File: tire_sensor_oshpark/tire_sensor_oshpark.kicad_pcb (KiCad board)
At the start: 4 copper layers, 33 x 26 mm, 40 parts, among them J1 Conn_02x05_Odd_Even, U2 DPS368, U3 LIS3DHTR, X1 32MHz, X2 32.768kHz

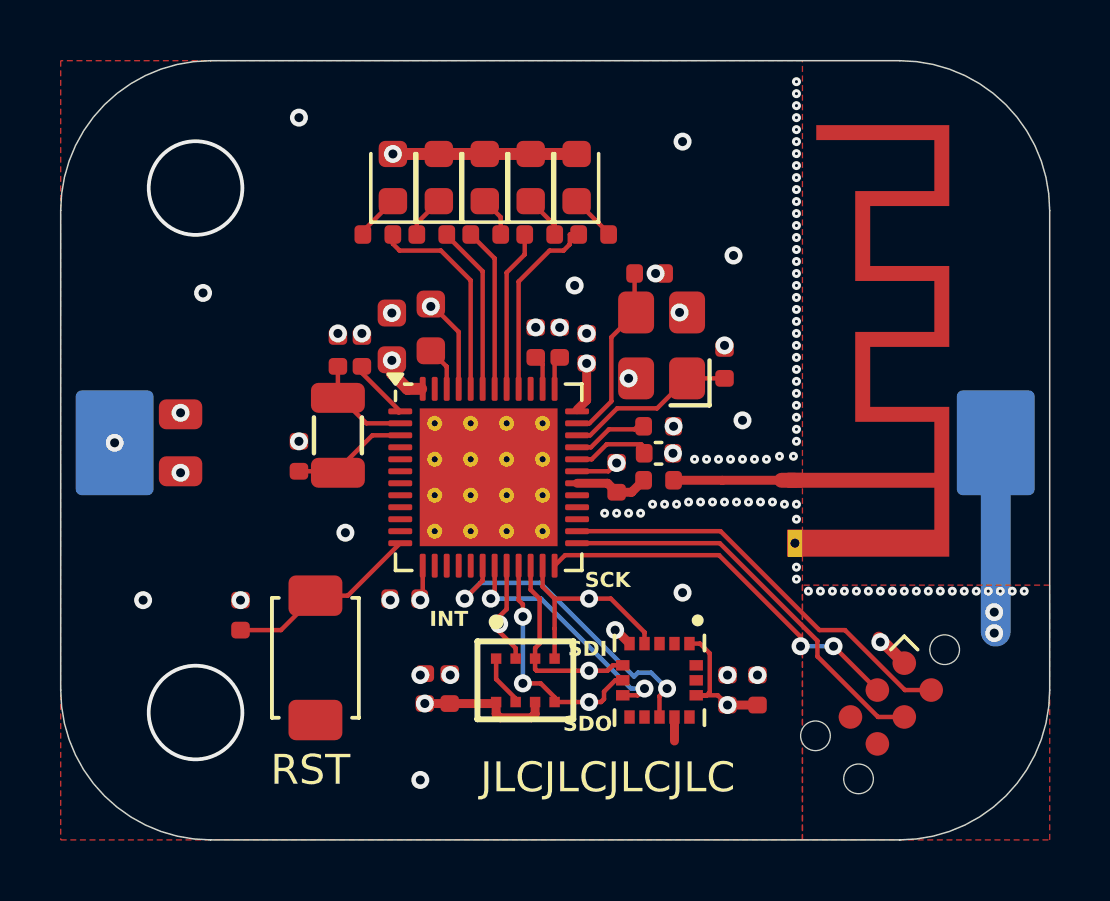
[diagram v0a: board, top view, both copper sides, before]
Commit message: Add OSHPark version, wider spacing
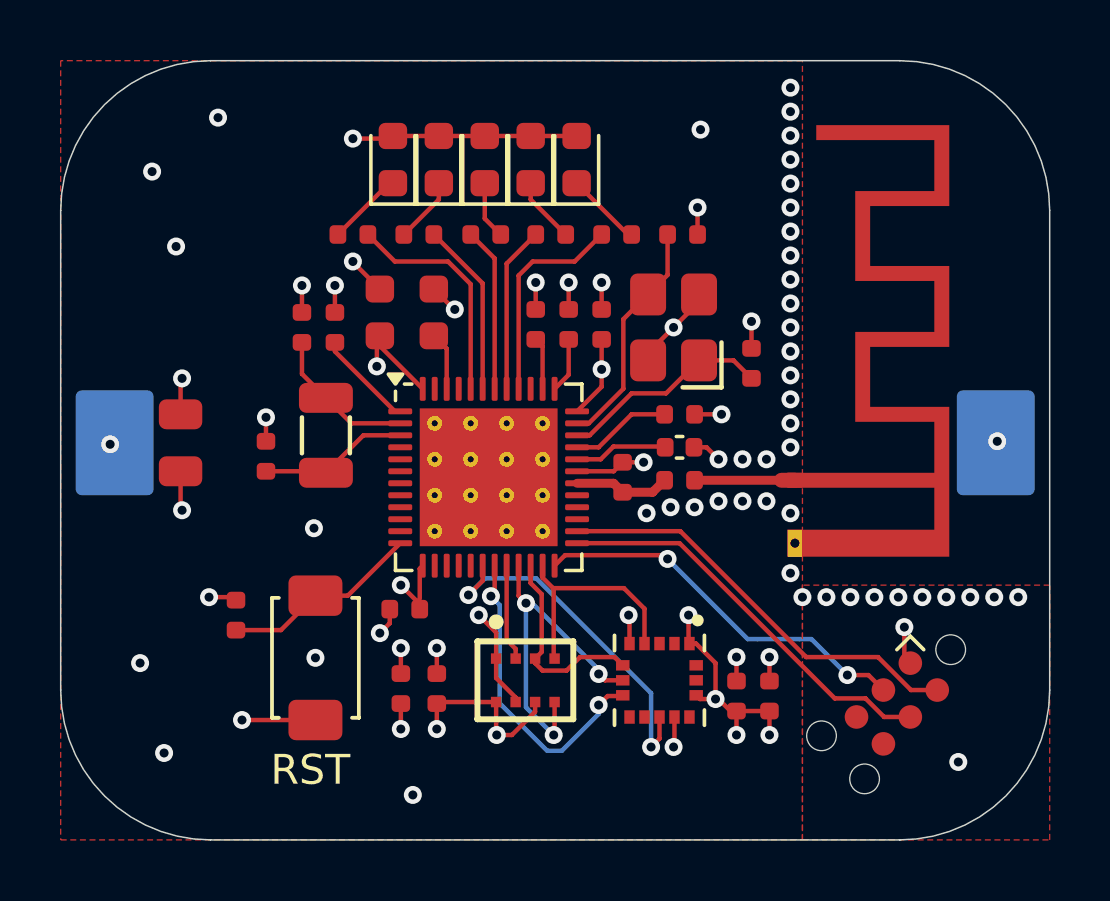
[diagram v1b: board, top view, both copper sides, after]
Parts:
- moved C2 1.70 mm to (176.6, 97.7)
- moved C11 1.44 mm to (163.9, 100.8)
- moved C4 1.20 mm to (165.0, 100.8)
- moved C12 1.10 mm to (162.7, 105.1)
- moved C8 0.94 mm to (173.9, 100.7)
- moved C1 0.90 mm to (178.9, 102.0)
- moved C9 0.89 mm to (166.5, 100.3)
- moved R5 0.83 mm to (165.6, 97.7)
- moved C7 0.81 mm to (176.5, 103.7)
- moved C19 0.80 mm to (167.2, 112.8)
- moved R1 0.77 mm to (174.4, 97.7)
- moved C6 0.73 mm to (176.5, 104.8)
- moved X1 0.72 mm to (176.3, 100.8)
- moved L1 0.70 mm to (176.5, 105.9)
- moved C13 0.67 mm to (172.8, 100.7)
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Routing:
- net GND: track 14.5 -> 29.6 mm, vias 115 -> 71
- net VDD_NRF: track 22.9 -> 33.6 mm, vias 10 -> 15
- net /SDO: track 8.12 -> 11.7 mm
- net /CS_LIS3DHTR: track 8.48 -> 10.5 mm
- net /XC2: track 6.08 -> 7.78 mm
- net /XC1: track 5.71 -> 7.10 mm
- net /P0.00/XL1: track 3.62 -> 5.01 mm
- net /P0.01/XL2: track 3.88 -> 5.02 mm
- net /DEC1: track 2.20 -> 3.31 mm
- net /INT_LIS3DHTR: track 10.9 -> 12.0 mm
- net Net-(D5-K): track 1.53 -> 2.54 mm
- net Net-(D1-K): track 1.55 -> 2.54 mm
- net /DEC3: track 2.59 -> 3.38 mm
- net Net-(D4-K): track 1.42 -> 2.20 mm
- net /RF: track 4.12 -> 3.35 mm
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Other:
- board text removed: "INT"
- board text removed: "JLCJLCJLCJLC"
- board text removed: "SCK"
- board text removed: "SDI"
- board text removed: "SDO"

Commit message: Fix VDD decoupling, reference docs
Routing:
- net VDD_NRF: track 33.6 -> 35.8 mm, vias 15 -> 12
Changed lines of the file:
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@@
-	)
-	(segment
-		(start 170.87156 114.390685)
-		(end 170.36656 114.390685)
-		(width 0.15)
-		(layer "F.Cu")
-		(net 1)
 	)
 	(segment
@@
 	)
 	(segment
-		(start 177.66656 113.190685)
-		(end 177.14656 113.190685)
-		(width 0.15)
-		(layer "F.Cu")
-		(net 1)
-	)
-	(segment
-		(start 178.36656 113.590685)
-		(end 178.16656 113.590685)
-		(width 0.15)
-		(layer "F.Cu")
-		(net 1)
-	)
-	(segment
 		(start 167.79656 109.840685)
 		(end 167.79656 108.840685)
@@
 	)
 	(segment
-		(start 176.79656 111.340685)
-		(end 177.01656 111.340685)
+		(start 177.96656 113.590685)
+		(end 178.36656 113.590685)
 		(width 0.15)
 		(layer "F.Cu")
@@
 	)
 	(segment
+		(start 177.11656 111.340685)
+		(end 177.56656 111.790685)
+		(width 0.15)
+		(layer "F.Cu")
+		(net 1)
+	)
+	(segment
+		(start 176.79656 111.340685)
+		(end 177.11656 111.340685)
+		(width 0.15)
+		(layer "F.Cu")
+		(net 1)
+	)
+	(segment
 		(start 173.86656 102.770685)
 		(end 173.86656 102.190685)
@@
 	)
 	(segment
-		(start 177.66656 111.990685)
-		(end 177.66656 113.190685)
-		(width 0.15)
-		(layer "F.Cu")
-		(net 1)
-	)
-	(segment
 		(start 177.14656 113.190685)
 		(end 177.02156 113.065685)
@@
 	)
 	(segment
-		(start 176.76656 110.390685)
-		(end 176.76656 111.310685)
-		(width 0.15)
-		(layer "F.Cu")
-		(net 1)
-	)
-	(segment
 		(start 168.36656 113.340685)
 		(end 168.36656 114.190685)
@@
 	)
 	(segment
+		(start 168.36656 113.340685)
+		(end 168.71756 113.691685)
+		(width 0.15)
+		(layer "F.Cu")
+		(net 1)
+	)
+	(segment
+		(start 173.36656 101.990685)
+		(end 173.36656 101.690685)
+		(width 0.15)
+		(layer "F.Cu")
+		(net 1)
+	)
+	(segment
 		(start 166.81406 94.490685)
 		(end 166.90156 94.403185)
@@
 	)
 	(segment
-		(start 171.64656 113.290685)
-		(end 171.64656 113.615685)
-		(width 0.15)
-		(layer "F.Cu")
-		(net 1)
-	)
-	(segment
 		(start 166.36656 102.090685)
 		(end 166.36656 101.170685)
@@
 	)
 	(segment
+		(start 177.56656 113.190685)
+		(end 177.14656 113.190685)
+		(width 0.15)
+		(layer "F.Cu")
+		(net 1)
+	)
+	(segment
+		(start 171.64656 113.615685)
+		(end 171.64656 113.290685)
+		(width 0.15)
+		(layer "F.Cu")
+		(net 1)
+	)
+	(segment
+		(start 171.57056 113.691685)
+		(end 171.64656 113.615685)
+		(width 0.15)
+		(layer "F.Cu")
+		(net 1)
+	)
+	(segment
 		(start 167.79656 110.020685)
 		(end 167.79656 110.190685)
@@
 	)
 	(segment
+		(start 168.71756 113.691685)
+		(end 171.57056 113.691685)
+		(width 0.15)
+		(layer "F.Cu")
+		(net 1)
+	)
+	(segment
 		(start 179.46656 114.390685)
 		(end 179.46656 113.590685)
@@
 	)
 	(segment
+		(start 177.56656 111.790685)
+		(end 177.56656 113.190685)
+		(width 0.15)
+		(layer "F.Cu")
+		(net 1)
+	)
+	(segment
 		(start 173.04656 103.590685)
 		(end 173.86656 102.770685)
@@
 	)
 	(segment
-		(start 170.34656 113.290685)
-		(end 170.34656 114.370685)
-		(width 0.15)
-		(layer "F.Cu")
-		(net 1)
-	)
-	(segment
-		(start 171.64656 113.615685)
-		(end 170.87156 114.390685)
+		(start 173.36656 101.690685)
+		(end 173.86656 101.190685)
 		(width 0.15)
 		(layer "F.Cu")
@@
 	(segment
 		(start 167.16656 113.340685)
+		(end 168.36656 113.340685)
+		(width 0.15)
+		(layer "F.Cu")
+		(net 1)
+	)
+	(segment
+		(start 167.16656 113.340685)
 		(end 167.16656 114.190685)
-		(width 0.15)
-		(layer "F.Cu")
-		(net 1)
-	)
-	(segment
-		(start 178.16656 113.590685)
-		(end 177.76656 113.190685)
 		(width 0.15)
 		(layer "F.Cu")
@@
 	)
 	(segment
-		(start 177.01656 111.340685)
-		(end 177.66656 111.990685)
-		(width 0.15)
-		(layer "F.Cu")
-		(net 1)
-	)
-	(segment
-		(start 170.34656 114.370685)
-		(end 170.36656 114.390685)
-		(width 0.15)
-		(layer "F.Cu")
-		(net 1)
-	)
-	(segment
 		(start 166.36656 101.170685)
 		(end 166.46656 101.070685)
@@
 	)
 	(segment
+		(start 177.56656 113.190685)
+		(end 177.96656 113.590685)
+		(width 0.15)
+		(layer "F.Cu")
+		(net 1)
+	)
+	(segment
 		(start 173.86656 101.190685)
 		(end 173.86656 102.190685)
@@
 	)
 	(via
-		(at 170.36656 114.390685)
-		(size 0.6)
-		(drill 0.3)
-		(layers "F.Cu" "B.Cu")
-		(free yes)
-		(net 1)
-	)
-	(via
-		(at 177.66656 113.190685)
-		(size 0.6)
-		(drill 0.3)
-		(layers "F.Cu" "B.Cu")
-		(free yes)
-		(net 1)
-	)
-	(via
 		(at 160.76656 109.790685)
 		(size 0.6)
@@
 	)
 	(via
+		(at 173.36656 101.990685)
+		(size 0.6)
+		(drill 0.3)
+		(layers "F.Cu" "B.Cu")
+		(free yes)
+		(net 1)
+	)
+	(via
 		(at 167.16656 114.190685)
 		(size 0.6)
@@
 	)
 	(via
-		(at 176.76656 110.390685)
-		(size 0.6)
-		(drill 0.3)
-		(layers "F.Cu" "B.Cu")
-		(free yes)
-		(net 1)
-	)
-	(via
 		(at 157.46656 104.690685)
 		(size 0.6)
 		(drill 0.3)
-		(layers "F.Cu" "B.Cu")
-		(free yes)
-		(net 1)
-	)
-	(via
-		(at 173.86656 102.190685)
-		(size 0.6)
-		(drill 0.3)

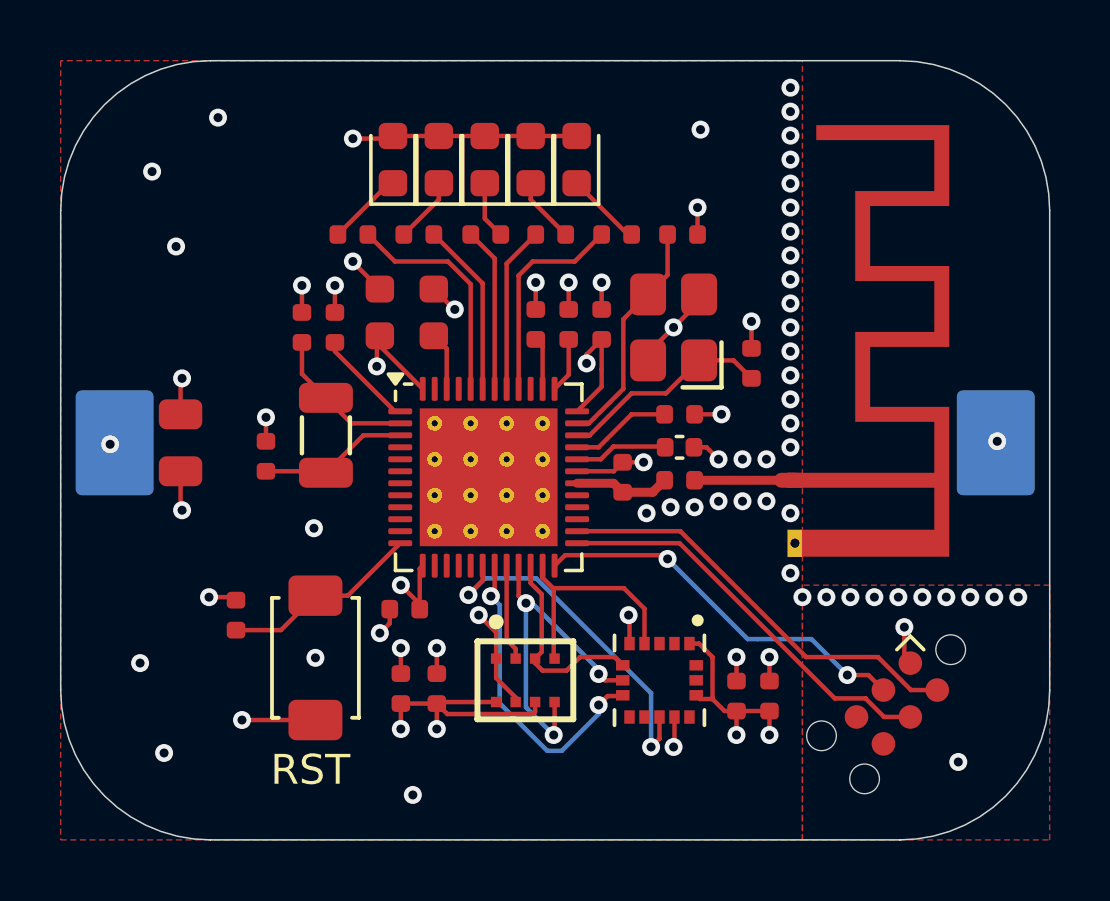
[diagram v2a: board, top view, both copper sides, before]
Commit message: Models, better decoupling
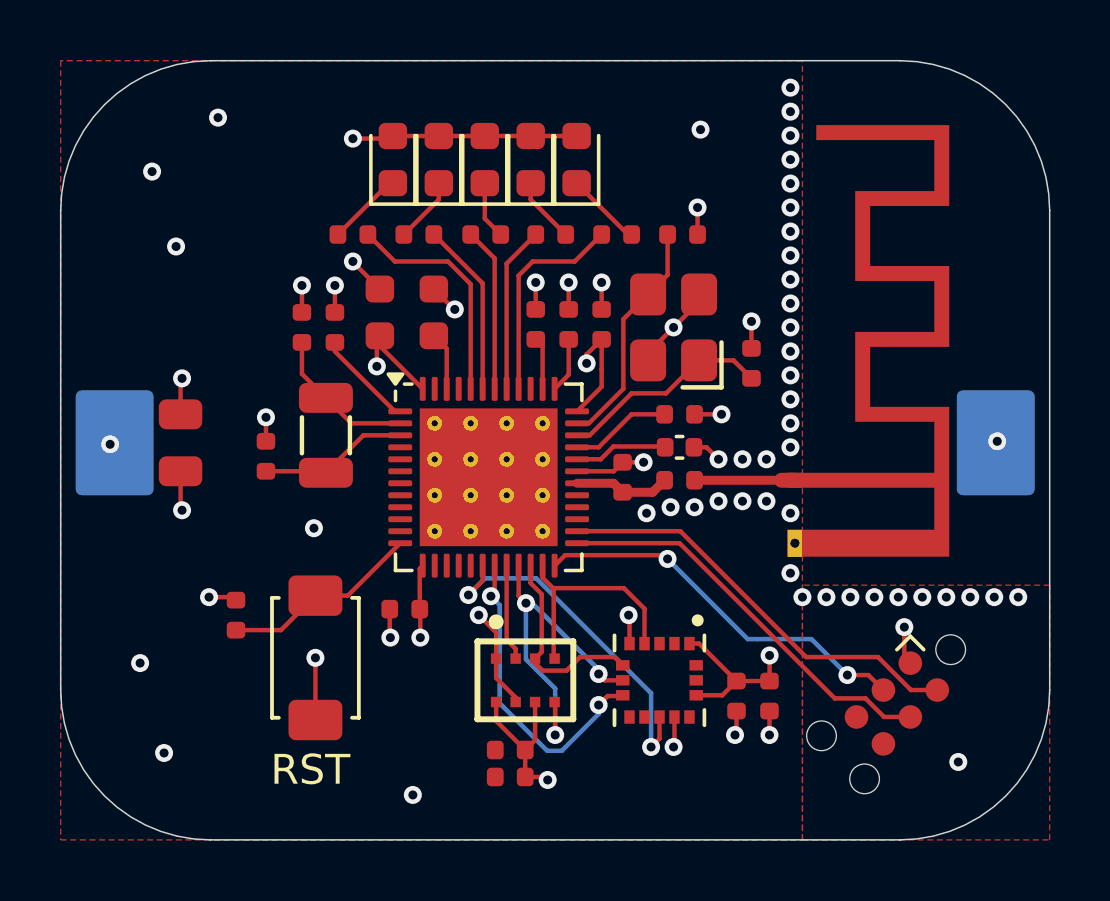
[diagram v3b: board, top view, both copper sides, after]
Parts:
- moved C19 4.69 mm to (170.8, 115.8), turned to 180 degrees
- moved C18 3.19 mm to (170.8, 114.9), turned to 180 degrees
- turned C16 to -90 degrees
- turned C17 to -90 degrees
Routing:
- net VDD_NRF: track 35.8 -> 31.3 mm, vias 12 -> 10
- net GND: track 29.6 -> 27.6 mm, vias 71 -> 68

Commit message: Add images
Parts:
- moved C19 0.10 mm to (170.8, 115.9)
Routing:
- net GND: track 27.6 -> 29.1 mm, vias 68 -> 70
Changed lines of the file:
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@@
 	(footprint "PCM_JLCPCB:C_0402"
 		(layer "F.Cu")
-		(at 170.81656 115.790685 180)
+		(at 170.81656 115.890685 180)
 		(descr "Capacitor SMD 0402 (1005 Metric), square (rectangular) end terminal, IPC_7351 nominal, (Body size source: IPC-SM-782 page 76, https://www.pcb-3d.com/wordpress/wp-content/uploads/ipc-sm-782a_amendment_1_and_2.pdf), generated with kicad-footprint-generator")
 		(tags "capacitor")
@@
 			)
 		)
+		(model "${KIPRJMOD}/models/BAT-HLD-013-SMT-TR.step"
+			(offset
+				(xyz 0 0 0)
+			)
+			(scale
+				(xyz 1 1 1)
+			)
+			(rotate
+				(xyz -90 -0 -0)
+			)
+		)
 	)
 	(gr_arc
@@
 	)
 	(segment
-		(start 172.06656 115.890685)
-		(end 171.96656 115.790685)
-		(width 0.15)
-		(layer "F.Cu")
-		(net 1)
-	)
-	(segment
 		(start 167.79656 109.840685)
 		(end 167.79656 108.840685)
@@
 	)
 	(segment
-		(start 171.31656 115.790685)
-		(end 171.31656 114.890685)
-		(width 0.15)
-		(layer "F.Cu")
-		(net 1)
-	)
-	(segment
 		(start 166.46656 101.410685)
 		(end 167.89656 102.840685)
@@
 	)
 	(segment
+		(start 171.31656 115.890685)
+		(end 171.31656 114.890685)
+		(width 0.15)
+		(layer "F.Cu")
+		(net 1)
+	)
+	(segment
 		(start 173.36656 101.690685)
 		(end 173.86656 101.190685)
@@
 	)
 	(segment
-		(start 171.96656 115.790685)
-		(end 171.31656 115.790685)
+		(start 172.06656 115.890685)
+		(end 171.31656 115.890685)
 		(width 0.15)
 		(layer "F.Cu")
@@
 	)
 	(segment
+		(start 169.56656 115.890685)
+		(end 170.31656 115.890685)
+		(width 0.15)
+		(layer "F.Cu")
+		(net 3)
+	)
+	(segment
 		(start 173.04656 105.590685)
 		(end 174.26656 105.590685)
@@
 		(net 3)
 	)
+	(segment
+		(start 169.56656 114.890685)
+		(end 170.31656 114.890685)
+		(width 0.15)
+		(layer "F.Cu")
+		(net 3)
+	)
 	(via
 		(at 180.16656 106.990685)
@@
 	)
 	(via
+		(at 169.56656 114.890685)
+		(size 0.6)
+		(drill 0.3)
+		(layers "F.Cu" "B.Cu")
+		(free yes)
+		(net 3)
+	)
+	(via
 		(at 158.46656 111.990685)
 		(size 0.6)
@@
 		(size 0.6)
 		(drill 0.3)
+		(layers "F.Cu" "B.Cu")
+		(free yes)
+		(net 3)
+	)
+	(via
+		(at 169.56656 115.890685)
+		(size 0.6)
+		(drill 0.3)
